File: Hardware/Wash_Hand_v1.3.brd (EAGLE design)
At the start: 71.1 x 48.3 mm, 64 parts, among them IC1 LM358D, IC2 LP298XS, IC3 4050D, J1 I2C, J2 ICSP, J3 SPI, J5 EXT_VCC, J6 6_PIN_SERIAL_CABLEPTH, Q1 16.0 Mhz, U1 328P

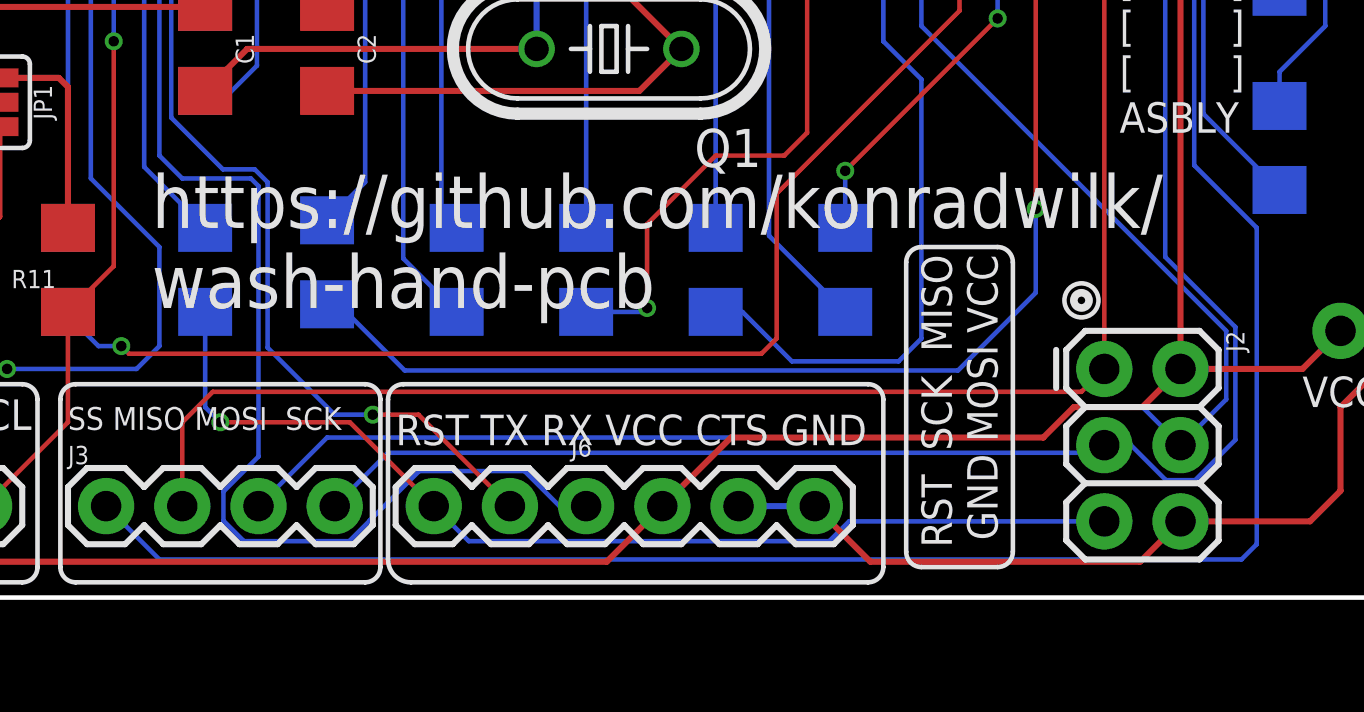
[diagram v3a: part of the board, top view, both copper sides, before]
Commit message: Board/Schematic: Use RESET instead of DTR on ICSP
We don't want the line past the 0.1uF cap to go
in the ICSP but instead use the one that goes directly
to the RESET pin.

Signed-off-by: Konrad Rzeszutek Wilk <konrad@kernel.org>
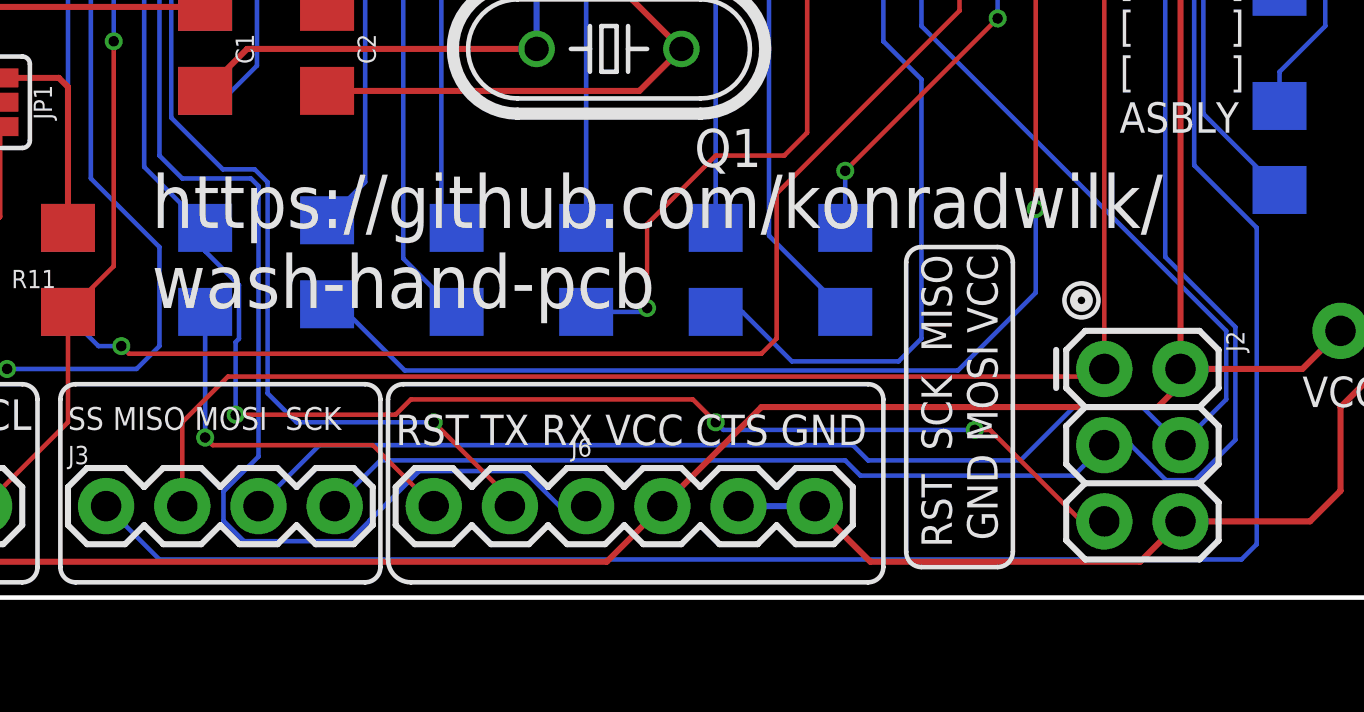
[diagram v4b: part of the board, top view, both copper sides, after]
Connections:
- net DTR: no longer J2.5
- net RESET: now also J2.5
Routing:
- net RESET: track 51.6 -> 89.2 mm, vias 0 -> 3
- net DTR: track 35.3 -> 12.8 mm
- net TX: track 31.7 -> 32.7 mm
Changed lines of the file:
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@@
 <wire x1="23.622" y1="40.386" x2="33.528" y2="40.386" width="0.1524" layer="1"/>
 <wire x1="33.528" y1="40.386" x2="36.192" y2="43.05" width="0.1524" layer="1"/>
+<contactref element="J2" pad="5"/>
+<wire x1="26.7826" y1="10.4166875" x2="26.7826" y2="8.6273125" width="0.1524" layer="16"/>
+<wire x1="25.654" y1="12.322" x2="25.654" y2="11.5452875" width="0.1524" layer="16"/>
+<wire x1="25.654" y1="11.5452875" x2="26.7826" y2="10.4166875" width="0.1524" layer="16"/>
+<wire x1="26.7826" y1="8.6273125" x2="26.67" y2="8.5147125" width="0.1524" layer="16"/>
+<wire x1="26.67" y1="8.5147125" x2="26.67" y2="6.096" width="0.1524" layer="16"/>
+<via x="26.67" y="6.096" extent="1-16" drill="0.35"/>
+<wire x1="26.67" y1="6.096" x2="32.004" y2="6.096" width="0.1524" layer="1"/>
+<wire x1="32.004" y1="6.096" x2="32.512" y2="6.604" width="0.1524" layer="1"/>
+<wire x1="32.512" y1="6.604" x2="41.91" y2="6.604" width="0.1524" layer="1"/>
+<wire x1="41.91" y1="6.604" x2="42.672" y2="5.842" width="0.1524" layer="1"/>
+<via x="42.672" y="5.842" extent="1-16" drill="0.35"/>
+<wire x1="42.672" y1="5.842" x2="42.926" y2="5.588" width="0.1524" layer="16"/>
+<wire x1="51.308" y1="5.588" x2="42.926" y2="5.588" width="0.1524" layer="16"/>
+<via x="51.308" y="5.588" extent="1-16" drill="0.35"/>
+<wire x1="54.864" y1="2.54" x2="51.816" y2="5.588" width="0.1524" layer="1"/>
+<wire x1="51.308" y1="5.588" x2="51.816" y2="5.588" width="0.1524" layer="1"/>
+<wire x1="54.864" y1="2.54" x2="55.626" y2="2.54" width="0.1524" layer="1"/>
 </signal>
 <signal name="VCC">
@@
 <wire x1="39.0398" y1="1.1938" x2="40.894" y2="3.048" width="0.2032" layer="1"/>
 <wire x1="13.0302" y1="1.1938" x2="39.0398" y2="1.1938" width="0.2032" layer="1"/>
-<wire x1="58.166" y1="7.62" x2="56.896" y2="6.35" width="0.2032" layer="1"/>
-<wire x1="56.896" y1="6.35" x2="54.61" y2="6.35" width="0.2032" layer="1"/>
-<wire x1="54.61" y1="6.35" x2="53.594" y2="5.334" width="0.2032" layer="1"/>
-<wire x1="43.18" y1="5.334" x2="40.894" y2="3.048" width="0.2032" layer="1"/>
-<wire x1="53.594" y1="5.334" x2="43.18" y2="5.334" width="0.2032" layer="1"/>
+<wire x1="58.166" y1="7.62" x2="58.166" y2="7.112" width="0.2032" layer="1"/>
+<wire x1="58.166" y1="7.112" x2="57.404" y2="6.35" width="0.2032" layer="1"/>
+<wire x1="57.404" y1="6.35" x2="44.196" y2="6.35" width="0.2032" layer="1"/>
+<wire x1="44.196" y1="6.35" x2="40.894" y2="3.048" width="0.2032" layer="1"/>
 <wire x1="18.796" y1="16.51" x2="17.018" y2="16.51" width="0.2032" layer="1"/>
 <wire x1="17.018" y1="16.51" x2="10.16" y2="9.652" width="0.2032" layer="1"/>
@@
 <contactref element="J3" pad="3"/>
 <contactref element="IC3" pad="5"/>
-<wire x1="27.432" y1="3.048" x2="29.718" y2="5.334" width="0.1524" layer="16"/>
-<wire x1="53.594" y1="5.334" x2="54.61" y2="6.35" width="0.1524" layer="16"/>
-<wire x1="54.61" y1="6.35" x2="56.896" y2="6.35" width="0.1524" layer="16"/>
+<wire x1="29.464" y1="5.08" x2="27.432" y2="3.048" width="0.1524" layer="16"/>
+<wire x1="56.896" y1="6.35" x2="54.61" y2="6.35" width="0.1524" layer="16"/>
 <wire x1="56.896" y1="6.35" x2="58.166" y2="5.08" width="0.1524" layer="16"/>
-<wire x1="29.718" y1="5.334" x2="53.594" y2="5.334" width="0.1524" layer="16"/>
 <wire x1="58.166" y1="5.08" x2="59.69" y2="6.604" width="0.1524" layer="16"/>
 <wire x1="59.69" y1="6.604" x2="59.69" y2="8.89" width="0.1524" layer="16"/>
@@
 <wire x1="23.9014" y1="35.0266" x2="28.448" y2="30.48" width="0.1524" layer="16"/>
 <wire x1="28.448" y1="30.48" x2="43.434" y2="30.48" width="0.1524" layer="16"/>
+<wire x1="52.832" y1="4.572" x2="47.752" y2="4.572" width="0.1524" layer="16"/>
+<wire x1="47.752" y1="4.572" x2="47.244" y2="5.08" width="0.1524" layer="16"/>
+<wire x1="47.244" y1="5.08" x2="29.464" y2="5.08" width="0.1524" layer="16"/>
+<wire x1="54.61" y1="6.35" x2="52.832" y2="4.572" width="0.1524" layer="16"/>
 </signal>
 <signal name="D1">
@@
 <wire x1="9.398" y1="37.592" x2="8.763" y2="38.227" width="0.1524" layer="1"/>
 <wire x1="8.763" y1="39.5986" x2="8.763" y2="38.227" width="0.1524" layer="1"/>
-<wire x1="55.626" y1="7.62" x2="54.864" y2="6.858" width="0.1524" layer="1"/>
-<wire x1="54.864" y1="6.858" x2="25.908" y2="6.858" width="0.1524" layer="1"/>
-<wire x1="25.908" y1="6.858" x2="24.892" y2="5.842" width="0.1524" layer="1"/>
+<wire x1="55.626" y1="7.62" x2="55.372" y2="7.366" width="0.1524" layer="1"/>
+<wire x1="55.372" y1="7.366" x2="26.416" y2="7.366" width="0.1524" layer="1"/>
+<wire x1="26.416" y1="7.366" x2="24.892" y2="5.842" width="0.1524" layer="1"/>
 <wire x1="24.892" y1="5.842" x2="24.892" y2="3.048" width="0.1524" layer="1"/>
 <via x="22.606" y="37.592" extent="1-16" drill="0.35"/>
@@
 <contactref element="J3" pad="4"/>
 <contactref element="IC3" pad="7"/>
-<wire x1="55.626" y1="5.08" x2="55.372" y2="4.826" width="0.1524" layer="16"/>
-<wire x1="31.75" y1="4.826" x2="29.972" y2="3.048" width="0.1524" layer="16"/>
-<wire x1="55.372" y1="4.826" x2="31.75" y2="4.826" width="0.1524" layer="16"/>
+<wire x1="31.496" y1="4.572" x2="29.972" y2="3.048" width="0.1524" layer="16"/>
 <wire x1="57.68203125" y1="3.9116" x2="58.64996875" y2="3.9116" width="0.1524" layer="16"/>
 <wire x1="59.9948" y1="9.01625625" x2="57.658" y2="11.35305625" width="0.1524" layer="16"/>
@@
 <via x="43.18" y="29.718" extent="1-16" drill="0.35"/>
 <wire x1="43.18" y1="29.718" x2="43.18" y2="35.052" width="0.1524" layer="1"/>
+<wire x1="47.498" y1="4.064" x2="54.61" y2="4.064" width="0.1524" layer="16"/>
+<wire x1="47.498" y1="4.064" x2="46.99" y2="4.572" width="0.1524" layer="16"/>
+<wire x1="46.99" y1="4.572" x2="31.496" y2="4.572" width="0.1524" layer="16"/>
+<wire x1="54.61" y1="4.064" x2="55.626" y2="5.08" width="0.1524" layer="16"/>
 </signal>
 <signal name="D4">
@@
 <signal name="DTR">
 <contactref element="C3" pad="1"/>
-<contactref element="J2" pad="5"/>
 <contactref element="J6" pad="DTR"/>
-<wire x1="55.626" y1="2.54" x2="47.11836875" y2="2.54" width="0.1524" layer="16"/>
-<wire x1="47.11836875" y1="2.54" x2="46.45796875" y2="1.8796" width="0.1524" layer="16"/>
-<wire x1="46.45796875" y1="1.8796" x2="34.4424" y2="1.8796" width="0.1524" layer="16"/>
-<wire x1="34.4424" y1="1.8796" x2="33.274" y2="3.048" width="0.1524" layer="16"/>
-<wire x1="33.274" y1="3.048" x2="30.48" y2="5.842" width="0.1524" layer="1"/>
-<wire x1="30.48" y1="5.842" x2="26.162" y2="5.842" width="0.1524" layer="1"/>
-<via x="26.162" y="5.842" extent="1-16" drill="0.35"/>
-<wire x1="26.162" y1="5.842" x2="25.654" y2="6.35" width="0.1524" layer="16"/>
-<wire x1="25.654" y1="6.35" x2="25.654" y2="9.522" width="0.1524" layer="16"/>
+<wire x1="33.274" y1="3.048" x2="31.242" y2="5.08" width="0.1524" layer="1"/>
+<wire x1="31.242" y1="5.08" x2="25.908" y2="5.08" width="0.1524" layer="1"/>
+<wire x1="25.908" y1="5.08" x2="25.654" y2="5.334" width="0.1524" layer="1"/>
+<via x="25.654" y="5.334" extent="1-16" drill="0.35"/>
+<wire x1="25.654" y1="5.334" x2="25.654" y2="9.522" width="0.1524" layer="16"/>
 </signal>
 <signal name="TX">
@@
 <contactref element="J6" pad="RXI"/>
 <wire x1="25.4" y1="27.432" x2="25.4" y2="24.8766875" width="0.1524" layer="16"/>
-<wire x1="27.7368" y1="8.3312" x2="29.972" y2="6.096" width="0.1524" layer="16"/>
+<wire x1="27.7368" y1="6.8072" x2="28.702" y2="5.842" width="0.1524" layer="16"/>
 <wire x1="27.30425625" y1="14.2748" x2="27.7368" y2="13.84225625" width="0.1524" layer="16"/>
-<wire x1="27.7368" y1="13.84225625" x2="27.7368" y2="8.3312" width="0.1524" layer="16"/>
+<wire x1="27.7368" y1="13.84225625" x2="27.7368" y2="6.8072" width="0.1524" layer="16"/>
 <wire x1="26.2439125" y1="14.2748" x2="27.30425625" y2="14.2748" width="0.1524" layer="16"/>
 <wire x1="24.5254" y1="15.9933125" x2="26.2439125" y2="14.2748" width="0.1524" layer="16"/>
 <wire x1="25.4" y1="24.8766875" x2="24.5254" y2="24.0020875" width="0.1524" layer="16"/>
 <wire x1="24.5254" y1="24.0020875" x2="24.5254" y2="15.9933125" width="0.1524" layer="16"/>
-<wire x1="29.972" y1="6.096" x2="31.242" y2="6.096" width="0.1524" layer="16"/>
-<via x="31.242" y="6.096" extent="1-16" drill="0.35"/>
-<wire x1="35.814" y1="3.048" x2="32.766" y2="6.096" width="0.1524" layer="1"/>
-<wire x1="32.766" y1="6.096" x2="31.242" y2="6.096" width="0.1524" layer="1"/>
+<wire x1="28.702" y1="5.842" x2="33.274" y2="5.842" width="0.1524" layer="16"/>
+<via x="33.274" y="5.842" extent="1-16" drill="0.35"/>
+<wire x1="35.814" y1="3.048" x2="35.814" y2="3.302" width="0.1524" layer="1"/>
+<wire x1="35.814" y1="3.302" x2="33.274" y2="5.842" width="0.1524" layer="1"/>
 </signal>
 <signal name="RX">

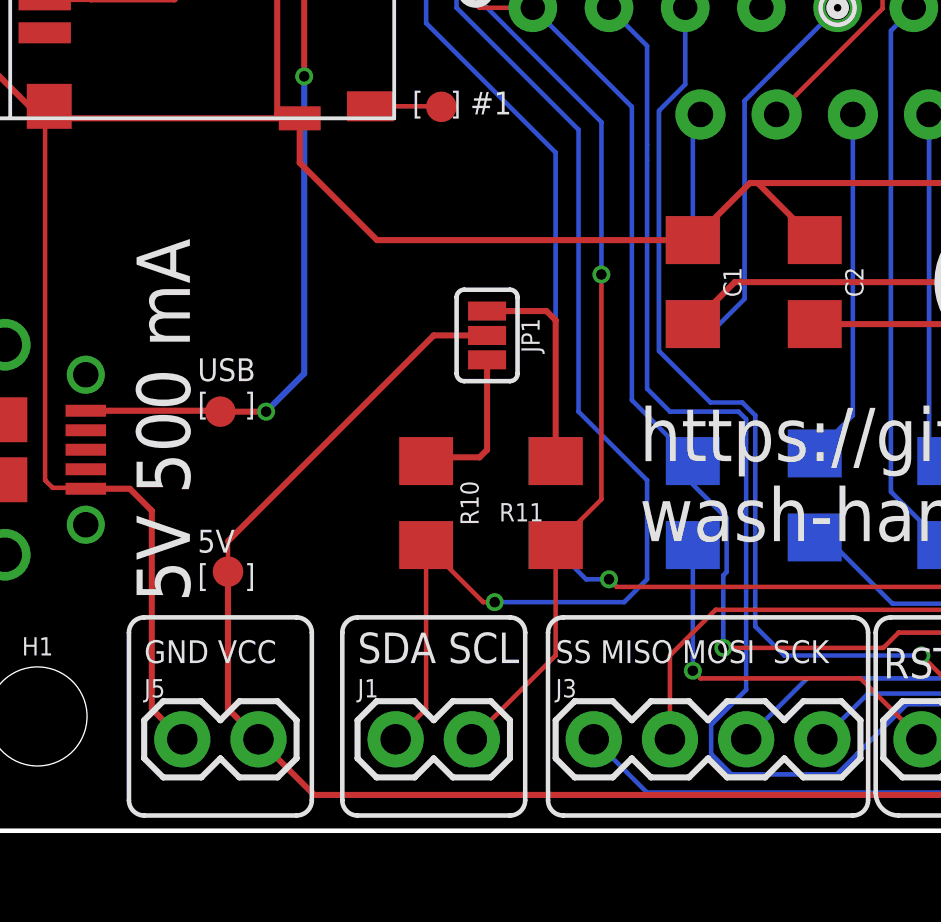
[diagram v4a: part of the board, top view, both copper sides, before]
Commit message: Board/Schematic: Add 1K resistor to DTR line
As a pull-down resistor to smooth down the DTR.

Signed-off-by: Konrad Rzeszutek Wilk <konrad@kernel.org>
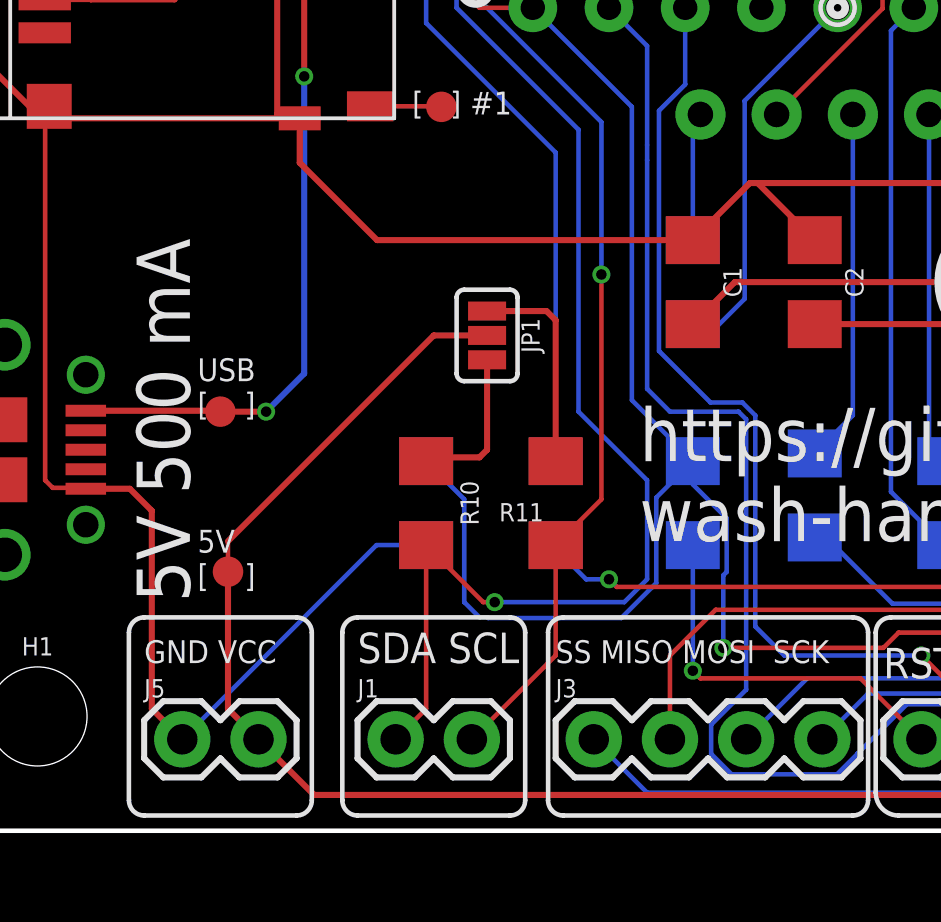
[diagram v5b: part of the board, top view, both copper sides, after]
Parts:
- added R12: 1K, darnok_common:1206
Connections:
- net 0: now also R12.1
- net RESET: now also R12.2
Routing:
- net RESET: track 89.2 -> 106.1 mm
- net 0: track 338.0 -> 348.8 mm
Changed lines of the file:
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@@
 <attribute name="REVISION" value="v1.3a.2" x="18.542" y="19.812" size="1.778" layer="28" rot="MR0" display="off"/>
+</element>
+<element name="R12" library="darnok_common" package="1206" value="1K" x="16.764" y="10.922" smashed="yes" rot="MR90">
+<attribute name="NAME" x="17.907" y="10.922" size="0.6096" layer="26" font="vector" ratio="20" rot="MR90" align="bottom-center"/>
+<attribute name="VALUE" x="15.621" y="10.922" size="0.6096" layer="28" font="vector" ratio="20" rot="MR90" align="top-center"/>
 </element>
 </elements>
@@
 <wire x1="51.308" y1="5.588" x2="51.816" y2="5.588" width="0.1524" layer="1"/>
 <wire x1="54.864" y1="2.54" x2="55.626" y2="2.54" width="0.1524" layer="1"/>
+<contactref element="R12" pad="2"/>
+<wire x1="25.654" y1="12.322" x2="24.4348" y2="11.1028" width="0.1524" layer="16"/>
+<wire x1="24.4348" y1="11.1028" x2="24.4348" y2="8.25574375" width="0.1524" layer="16"/>
+<wire x1="18.8302125" y1="7.0894" x2="18.8076125" y2="7.112" width="0.1524" layer="16"/>
+<wire x1="24.4348" y1="8.25574375" x2="23.26845625" y2="7.0894" width="0.1524" layer="16"/>
+<wire x1="23.26845625" y1="7.0894" x2="18.8302125" y2="7.0894" width="0.1524" layer="16"/>
+<wire x1="18.8076125" y1="7.112" x2="18.542" y2="7.112" width="0.1524" layer="16"/>
+<wire x1="18.542" y1="7.112" x2="18.034" y2="7.62" width="0.1524" layer="16"/>
+<wire x1="18.034" y1="11.052" x2="16.764" y2="12.322" width="0.1524" layer="16"/>
+<wire x1="18.034" y1="7.62" x2="18.034" y2="11.052" width="0.1524" layer="16"/>
 </signal>
 <signal name="VCC">
@@
 <wire x1="12.55" y1="22.265840625" x2="15.127840625" y2="19.688" width="0.2032" layer="1"/>
 <wire x1="25.654" y1="19.688" x2="27.556" y2="21.59" width="0.2032" layer="1"/>
-<wire x1="27.556" y1="21.59" x2="27.686" y2="21.59" width="0.2032" layer="1"/>
 <wire x1="29.718" y1="19.688" x2="27.816" y2="21.59" width="0.2032" layer="1"/>
-<wire x1="27.816" y1="21.59" x2="27.686" y2="21.59" width="0.2032" layer="1"/>
+<wire x1="27.816" y1="21.59" x2="27.556" y2="21.59" width="0.2032" layer="1"/>
+<contactref element="R12" pad="1"/>
+<wire x1="16.764" y1="9.522" x2="15.11" y2="9.522" width="0.1524" layer="16"/>
+<wire x1="15.11" y1="9.522" x2="8.636" y2="3.048" width="0.1524" layer="16"/>
 </signal>
 <signal name="D0">
